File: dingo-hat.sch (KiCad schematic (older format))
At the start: 54 parts, among them J1 LiPo-Power, J10 PJ-037B, J11 Bypass-Power, J12 Chassis-Out, J13 i2c_display, J14 NEOPIXEL, J15 MPU-9250, J2 Raspberry_Pi_2_3, J24 3mm_Mount, J25 3mm_Mount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

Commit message: Doing some back and forth on initial placements. Remove address options for PWM.
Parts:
- removed JP3: A1, Jumper:SolderJumper-2_P1.3mm_Open_RoundedPad1.0x1.5mm, symbol Jumper:SolderJumper_2_Open
- removed JP4: A2, Jumper:SolderJumper-2_P1.3mm_Open_RoundedPad1.0x1.5mm, symbol Jumper:SolderJumper_2_Open
- removed RN5: 10K_Pack04, Resistor_SMD:R_Array_Convex_4x0603, symbol Device:R_Pack04
- added R?: 10K, Resistors_SMD:R_0603, symbol Device:R
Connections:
- net A1 is gone; now on net GND: U2.2 (A1)
- net A2 is gone; now on net GND: U2.3 (A2)
- net A0: now also R?.1
- net GND: now also R?.2
- no-connect marks 6 -> 5
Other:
- moved on the sheet: JP2
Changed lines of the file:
@@
 Wire Wire Line
 	8600 1900 8600 1950
-Wire Wire Line
-	9100 3250 8850 3250
 Text Label 8850 3250 0    50   ~ 0
 A0
-Wire Wire Line
-	9100 3350 8850 3350
 Text Label 8850 3350 0    50   ~ 0
 A1
-Wire Wire Line
-	9100 3450 8850 3450
 Text Label 8850 3450 0    50   ~ 0
 A2
@@
 L power:+3.3V #PWR0106
 U 1 1 5C0019DB
-P 9100 4850
-F 0 "#PWR0106" H 9100 4700 50  0001 C CNN
-F 1 "+3.3V" H 9115 5023 50  0000 C CNN
-F 2 "" H 9100 4850 50  0001 C CNN
-F 3 "" H 9100 4850 50  0001 C CNN
-	1    9100 4850
+P 8450 2650
+F 0 "#PWR0106" H 8450 2500 50  0001 C CNN
+F 1 "+3.3V" H 8465 2823 50  0000 C CNN
+F 2 "" H 8450 2650 50  0001 C CNN
+F 3 "" H 8450 2650 50  0001 C CNN
+	1    8450 2650
 	1    0    0    -1
 $EndComp
@@
 L Jumper:SolderJumper_2_Open JP2
 U 1 1 5C001CDA
-P 9650 5000
-F 0 "JP2" H 9550 5050 50  0000 C CNN
-F 1 "A0" H 9750 5050 50  0000 C CNN
-F 2 "Jumper:SolderJumper-2_P1.3mm_Open_RoundedPad1.0x1.5mm" H 9650 5000 50  0001 C CNN
-F 3 "~" H 9650 5000 50  0001 C CNN
-	1    9650 5000
-	1    0    0    -1
-$EndComp
-$Comp
-L Jumper:SolderJumper_2_Open JP3
-U 1 1 5C0024E7
-P 9400 5100
-F 0 "JP3" H 9300 5150 50  0000 C CNN
-F 1 "A1" H 9500 5150 50  0000 C CNN
-F 2 "Jumper:SolderJumper-2_P1.3mm_Open_RoundedPad1.0x1.5mm" H 9400 5100 50  0001 C CNN
-F 3 "~" H 9400 5100 50  0001 C CNN
-	1    9400 5100
-	1    0    0    -1
-$EndComp
-$Comp
-L Jumper:SolderJumper_2_Open JP4
-U 1 1 5C002617
-P 9650 5200
-F 0 "JP4" H 9550 5250 50  0000 C CNN
-F 1 "A2" H 9750 5250 50  0000 C CNN
-F 2 "Jumper:SolderJumper-2_P1.3mm_Open_RoundedPad1.0x1.5mm" H 9650 5200 50  0001 C CNN
-F 3 "~" H 9650 5200 50  0001 C CNN
-	1    9650 5200
-	1    0    0    -1
+P 8450 2950
+F 0 "JP2" H 8350 3000 50  0000 C CNN
+F 1 "A0" H 8550 3000 50  0000 C CNN
+F 2 "Jumper:SolderJumper-2_P1.3mm_Open_RoundedPad1.0x1.5mm" H 8450 2950 50  0001 C CNN
+F 3 "~" H 8450 2950 50  0001 C CNN
+	1    8450 2950
+	0    -1   1    0
 $EndComp
 $Comp
@@
 $EndComp
 NoConn ~ 550  6700
-$Comp
-L Device:R_Pack04 RN5
-U 1 1 5C4B78BC
-P 10300 5100
-F 0 "RN5" V 9883 5100 50  0000 C CNN
-F 1 "10K_Pack04" V 9974 5100 50  0000 C CNN
-F 2 "Resistor_SMD:R_Array_Convex_4x0603" V 10575 5100 50  0001 C CNN
-F 3 "~" H 10300 5100 50  0001 C CNN
-F 4 "SMD" H 0   0   50  0001 C CNN "Package"
-	1    10300 5100
-	0    1    -1   0
-$EndComp
-Wire Wire Line
-	9100 4850 9100 5000
-Wire Wire Line
-	9100 5000 9500 5000
-Connection ~ 9100 5000
-Wire Wire Line
-	9100 5000 9100 5100
-Wire Wire Line
-	9250 5100 9100 5100
-Connection ~ 9100 5100
-Wire Wire Line
-	9100 5100 9100 5200
-Wire Wire Line
-	9500 5200 9100 5200
-Wire Wire Line
-	10500 5000 10600 5000
-Wire Wire Line
-	10600 5000 10600 5100
-Wire Wire Line
-	10500 5300 10600 5300
-Wire Wire Line
-	10500 5200 10600 5200
-Connection ~ 10600 5200
-Wire Wire Line
-	10600 5200 10600 5300
-Wire Wire Line
-	10500 5100 10600 5100
-Connection ~ 10600 5100
-Wire Wire Line
-	10600 5100 10600 5200
-Wire Wire Line
-	10100 5000 9800 5000
-Wire Wire Line
-	10100 5100 9550 5100
-Wire Wire Line
-	9800 5200 10100 5200
-NoConn ~ 10100 5300
-Text Label 9900 5000 0    50   ~ 0
-A0
-Text Label 9900 5100 0    50   ~ 0
-A1
-Text Label 9900 5200 0    50   ~ 0
-A2
+Wire Wire Line
+	8450 2650 8450 2800
 $Comp
 L Device:C C9
@@
 Text Notes 5500 5550 0    50   ~ 0
 ADC
-Text Notes 5650 6650 0    50   ~ 0
+Text Notes 4200 7500 0    50   ~ 0
 i2c Addresses:\nPCA9685PW --\nMPU-9250 --\nMPC3021 --\nDisplay --
-$Comp
-L power:GND #PWR011
-U 1 1 5E262FFC
-P 10600 5300
-F 0 "#PWR011" H 10600 5050 50  0001 C CNN
-F 1 "GND" H 10605 5127 50  0000 C CNN
-F 2 "" H 10600 5300 50  0001 C CNN
-F 3 "" H 10600 5300 50  0001 C CNN
-	1    10600 5300
-	1    0    0    -1
-$EndComp
-Connection ~ 10600 5300
 $Comp
 L power:GND #PWR010
@@
 Wire Wire Line
 	1150 5300 1250 5300
+$Comp
+L Device:R R?
+U 1 1 5E332011
+P 8450 3500
+F 0 "R?" H 8520 3546 50  0000 L CNN
+F 1 "10K" H 8520 3455 50  0000 L CNN
+F 2 "Resistors_SMD:R_0603" V 8380 3500 50  0001 C CNN
+F 3 "~" H 8450 3500 50  0001 C CNN
+F 4 "0603" H -300 650 50  0001 C CNN "Package"
+	1    8450 3500
+	1    0    0    -1
+$EndComp
+Wire Wire Line
+	8800 3550 8800 3450
+Wire Wire Line
+	8800 3450 9100 3450
+Connection ~ 8800 3550
+Wire Wire Line
+	8800 3350 8800 3450
+Wire Wire Line
+	8800 3350 9100 3350
+Connection ~ 8800 3450
+Wire Wire Line
+	8450 3250 8450 3100
+Wire Wire Line
+	8450 3350 8450 3250
+Connection ~ 8450 3250
+Wire Wire Line
+	8450 3250 9100 3250
+$Comp
+L power:GND #PWR?
+U 1 1 5E42228B
+P 8450 3850
+F 0 "#PWR?" H 8450 3600 50  0001 C CNN
+F 1 "GND" H 8455 3677 50  0000 C CNN
+F 2 "" H 8450 3850 50  0001 C CNN
+F 3 "" H 8450 3850 50  0001 C CNN
+	1    8450 3850
+	1    0    0    -1
+$EndComp
+Wire Wire Line
+	8450 3650 8450 3850
 $EndSCHEMATC

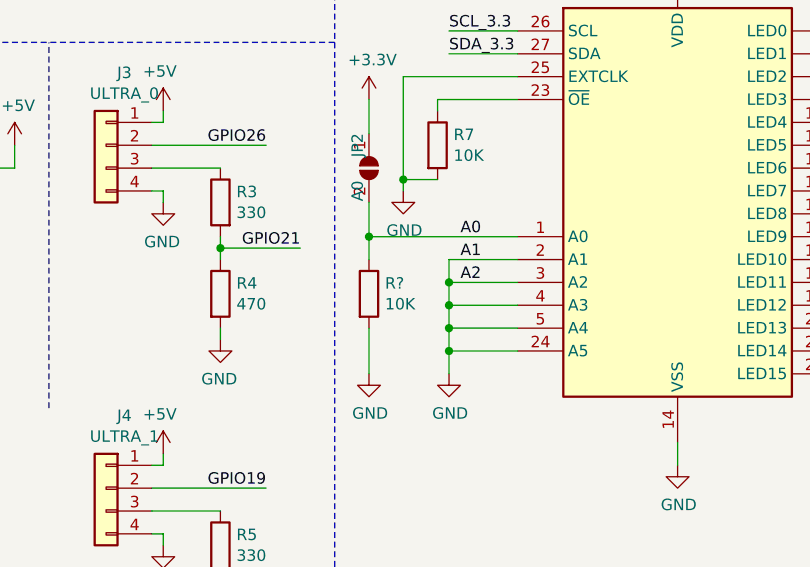
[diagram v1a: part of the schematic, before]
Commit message: Trying out layout, modifying solder pad footprint.
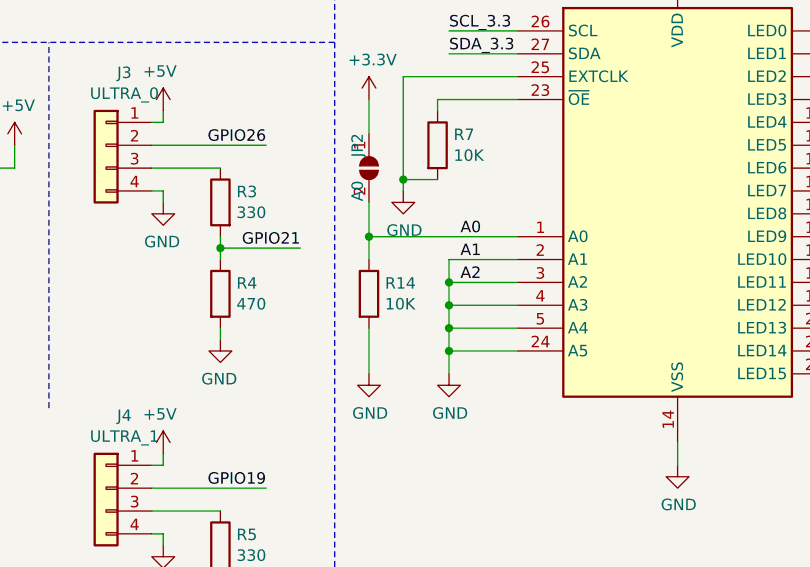
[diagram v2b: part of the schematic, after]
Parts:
- gave numbers to parts that had none: 1
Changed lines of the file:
@@
 	1150 5300 1250 5300
 $Comp
-L Device:R R?
+L Device:R R14
 U 1 1 5E332011
 P 8450 3500
-F 0 "R?" H 8520 3546 50  0000 L CNN
+F 0 "R14" H 8520 3546 50  0000 L CNN
 F 1 "10K" H 8520 3455 50  0000 L CNN
 F 2 "Resistors_SMD:R_0603" V 8380 3500 50  0001 C CNN
@@
 	8450 3250 9100 3250
 $Comp
-L power:GND #PWR?
+L power:GND #PWR0107
 U 1 1 5E42228B
 P 8450 3850
-F 0 "#PWR?" H 8450 3600 50  0001 C CNN
+F 0 "#PWR0107" H 8450 3600 50  0001 C CNN
 F 1 "GND" H 8455 3677 50  0000 C CNN
 F 2 "" H 8450 3850 50  0001 C CNN

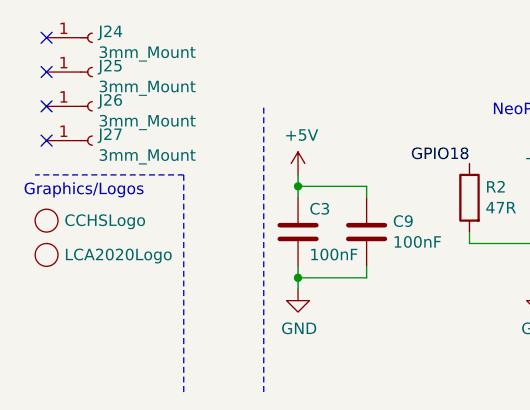
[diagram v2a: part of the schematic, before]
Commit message: Updated for the logo.
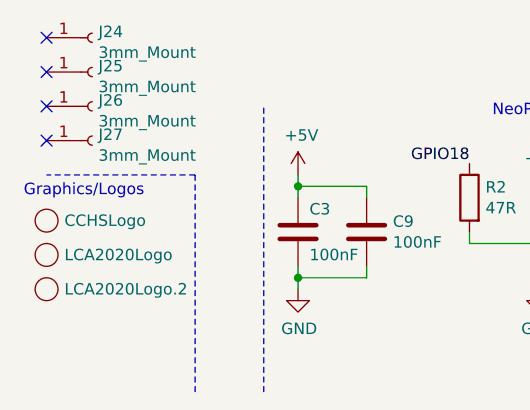
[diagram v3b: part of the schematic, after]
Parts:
- added G3: LCA2020Logo.2, libs:logo.LCA.2020.2, symbol dingo-hat-graphics:LCA2020Logo
- G2: footprint (none) -> libs:logo.LCA.2020.1
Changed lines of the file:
@@
 Connection ~ 4000 850
 Wire Notes Line
-	1150 7800 1150 6850
+	1200 7800 1200 6850
 Wire Notes Line
-	1150 6850 500  6850
+	1200 6850 550  6850
 Text Notes 450  6950 0    50   ~ 0
 Graphics/Logos
@@
 F 0 "G2" H 628 7200 50  0001 L CNN
 F 1 "LCA2020Logo" H 628 7200 50  0000 L CNN
-F 2 "" H 550 7200 50  0001 C CNN
+F 2 "libs:logo.LCA.2020.1" H 550 7200 50  0001 C CNN
 F 3 "" H 550 7200 50  0001 C CNN
 	1    550  7200
@@
 Wire Wire Line
 	8450 3650 8450 3850
+$Comp
+L dingo-hat-graphics:LCA2020Logo G3
+U 1 1 5DBE0FB1
+P 550 7350
+F 0 "G3" H 628 7350 50  0001 L CNN
+F 1 "LCA2020Logo.2" H 628 7350 50  0000 L CNN
+F 2 "libs:logo.LCA.2020.2" H 550 7350 50  0001 C CNN
+F 3 "" H 550 7350 50  0001 C CNN
+	1    550  7350
+	1    0    0    -1
+$EndComp
 $EndSCHEMATC

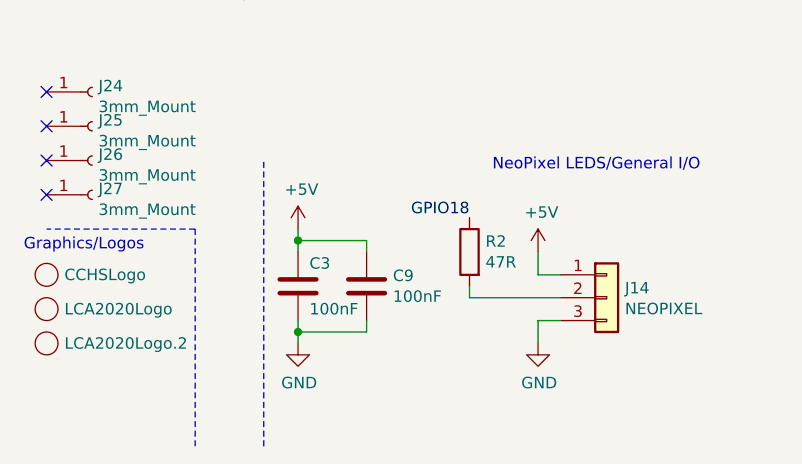
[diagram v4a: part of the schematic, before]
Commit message: Needs cleaning up, but most routing done.
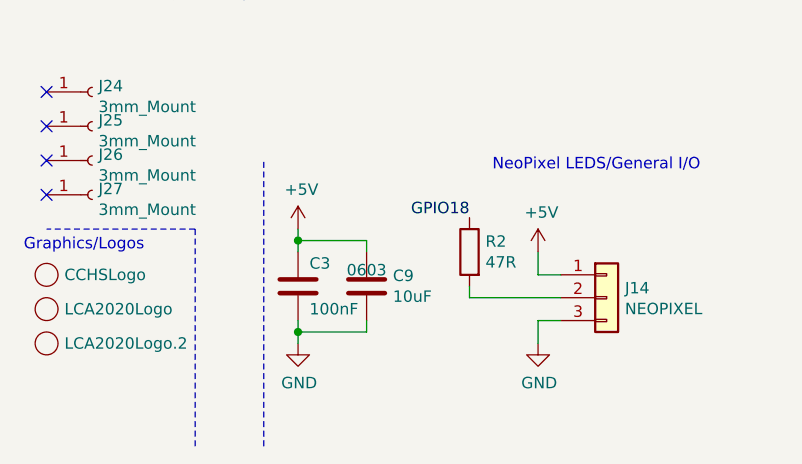
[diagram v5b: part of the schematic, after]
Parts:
- C3: footprint Capacitor_SMD:C_0603_1608Metric_Pad1.05x0.95mm_HandSolder -> Resistors_SMD:R_0603
- C9: value 100nF -> 10uF; footprint Capacitor_SMD:C_0603_1608Metric_Pad1.05x0.95mm_HandSolder -> Resistors_SMD:R_0603; Description CAP CER 0.1UF 50V X7R 0603 -> (none); Link https://www.digikey.com/product-detail/en/samsung-electro-m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 -> (none); Supplier 1 Digi-Key -> (none); Supplier Part Number 1 1276-1000-1-ND -> (none); Unit Cost A$ 0.15000 -> (none); Voltage Rating 50V -> (none)
- R10, R11, R8, R9: footprint Resistor_SMD:R_0603_1608Metric_Pad1.05x0.95mm_HandSolder -> Resistors_SMD:R_0603
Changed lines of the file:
@@
-$EndComp
-$Comp
-L Device:C C3
-U 1 1 5C14B529
-P 1650 7100
-F 0 "C3" H 1700 7200 50  0000 L CNN
-F 1 "100nF" H 1700 7000 50  0000 L CNN
-F 2 "Capacitor_SMD:C_0603_1608Metric_Pad1.05x0.95mm_HandSolder" H 1688 6950 50  0001 C CNN
-F 3 "~" H 1650 7100 50  0001 C CNN
-F 4 "0603" H -1650 -50 50  0001 C CNN "Package"
-F 5 "CAP CER 0.1UF 50V X7R 0603" H 1650 7100 50  0001 C CNN "Description"
-F 6 "50V" H 1650 7100 50  0001 C CNN "Voltage Rating"
-F 7 "https://www.digikey.com/product-detail/en/samsung-electro-mechanics/CL10B104KB8NNNC/1276-1000-1-ND/3889086" H 1650 7100 50  0001 C CNN "Link"
-F 8 "Digi-Key" H 1650 7100 50  0001 C CNN "Supplier 1"
-F 9 "1276-1000-1-ND" H 1650 7100 50  0001 C CNN "Supplier Part Number 1"
-F 10 "0.15000" H 1650 7100 50  0001 C CNN "Unit Cost A$"
-	1    1650 7100
-	1    0    0    -1
 $EndComp
 $Comp
@@
 Wire Wire Line
 	8450 2650 8450 2800
-$Comp
-L Device:C C9
-U 1 1 5CC83074
-P 1950 7100
-F 0 "C9" H 2065 7146 50  0000 L CNN
-F 1 "100nF" H 2065 7055 50  0000 L CNN
-F 2 "Capacitor_SMD:C_0603_1608Metric_Pad1.05x0.95mm_HandSolder" H 1988 6950 50  0001 C CNN
-F 3 "~" H 1950 7100 50  0001 C CNN
-F 4 "0603" H -1650 -50 50  0001 C CNN "Package"
-F 5 "CAP CER 0.1UF 50V X7R 0603" H 1950 7100 50  0001 C CNN "Description"
-F 6 "50V" H 1950 7100 50  0001 C CNN "Voltage Rating"
-F 7 "https://www.digikey.com/product-detail/en/samsung-electro-mechanics/CL10B104KB8NNNC/1276-1000-1-ND/3889086" H 1950 7100 50  0001 C CNN "Link"
-F 8 "Digi-Key" H 1950 7100 50  0001 C CNN "Supplier 1"
-F 9 "1276-1000-1-ND" H 1950 7100 50  0001 C CNN "Supplier Part Number 1"
-F 10 "0.15000" H 1950 7100 50  0001 C CNN "Unit Cost A$"
-	1    1950 7100
-	1    0    0    -1
-$EndComp
 Wire Wire Line
 	1950 6950 1950 6900
@@
 F 0 "R8" H 3170 1096 50  0000 L CNN
 F 1 "3.9K" H 3170 1005 50  0000 L CNN
-F 2 "Resistor_SMD:R_0603_1608Metric_Pad1.05x0.95mm_HandSolder" V 3030 1050 50  0001 C CNN
+F 2 "Resistors_SMD:R_0603" V 3030 1050 50  0001 C CNN
 F 3 "~" H 3100 1050 50  0001 C CNN
 F 4 "0603" H 3100 1050 50  0001 C CNN "Package"
@@
 F 0 "R9" H 3470 1096 50  0000 L CNN
 F 1 "3.9K" H 3470 1005 50  0000 L CNN
-F 2 "Resistor_SMD:R_0603_1608Metric_Pad1.05x0.95mm_HandSolder" V 3330 1050 50  0001 C CNN
+F 2 "Resistors_SMD:R_0603" V 3330 1050 50  0001 C CNN
 F 3 "~" H 3400 1050 50  0001 C CNN
 F 4 "0603" H 3400 1050 50  0001 C CNN "Package"
@@
 F 0 "R10" H 3770 1096 50  0000 L CNN
 F 1 "3.9K" H 3770 1005 50  0000 L CNN
-F 2 "Resistor_SMD:R_0603_1608Metric_Pad1.05x0.95mm_HandSolder" V 3630 1050 50  0001 C CNN
+F 2 "Resistors_SMD:R_0603" V 3630 1050 50  0001 C CNN
 F 3 "~" H 3700 1050 50  0001 C CNN
 F 4 "0603" H 0   0   50  0001 C CNN "Package"
@@
 F 0 "R11" H 4070 1096 50  0000 L CNN
 F 1 "3.9K" H 4070 1005 50  0000 L CNN
-F 2 "Resistor_SMD:R_0603_1608Metric_Pad1.05x0.95mm_HandSolder" V 3930 1050 50  0001 C CNN
+F 2 "Resistors_SMD:R_0603" V 3930 1050 50  0001 C CNN
 F 3 "~" H 4000 1050 50  0001 C CNN
 F 4 "0603" H 0   0   50  0001 C CNN "Package"
@@
 F2 "BatterySupply" I L 5150 4600 50
 $EndSheet
+$Comp
+L Device:C C9
+U 1 1 5E5C23D5
+P 1950 7100
+F 0 "C9" H 2065 7146 50  0000 L CNN
+F 1 "10uF" H 2065 7055 50  0000 L CNN
+F 2 "Resistors_SMD:R_0603" H 1988 6950 50  0001 C CNN
+F 3 "~" H 1950 7100 50  0001 C CNN
+F 4 "0603" H 1950 7200 50  0000 C TNN "Package"
+	1    1950 7100
+	1    0    0    -1
+$EndComp
+$Comp
+L Device:C C3
+U 1 1 5C14B529
+P 1650 7100
+F 0 "C3" H 1700 7200 50  0000 L CNN
+F 1 "100nF" H 1700 7000 50  0000 L CNN
+F 2 "Resistors_SMD:R_0603" H 1688 6950 50  0001 C CNN
+F 3 "~" H 1650 7100 50  0001 C CNN
+F 4 "0603" H -1650 -50 50  0001 C CNN "Package"
+F 5 "CAP CER 0.1UF 50V X7R 0603" H 1650 7100 50  0001 C CNN "Description"
+F 6 "50V" H 1650 7100 50  0001 C CNN "Voltage Rating"
+F 7 "https://www.digikey.com/product-detail/en/samsung-electro-mechanics/CL10B104KB8NNNC/1276-1000-1-ND/3889086" H 1650 7100 50  0001 C CNN "Link"
+F 8 "Digi-Key" H 1650 7100 50  0001 C CNN "Supplier 1"
+F 9 "1276-1000-1-ND" H 1650 7100 50  0001 C CNN "Supplier Part Number 1"
+F 10 "0.15000" H 1650 7100 50  0001 C CNN "Unit Cost A$"
+	1    1650 7100
+	1    0    0    -1
+$EndComp
 $EndSCHEMATC
